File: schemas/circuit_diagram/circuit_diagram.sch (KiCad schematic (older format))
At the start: 10 parts

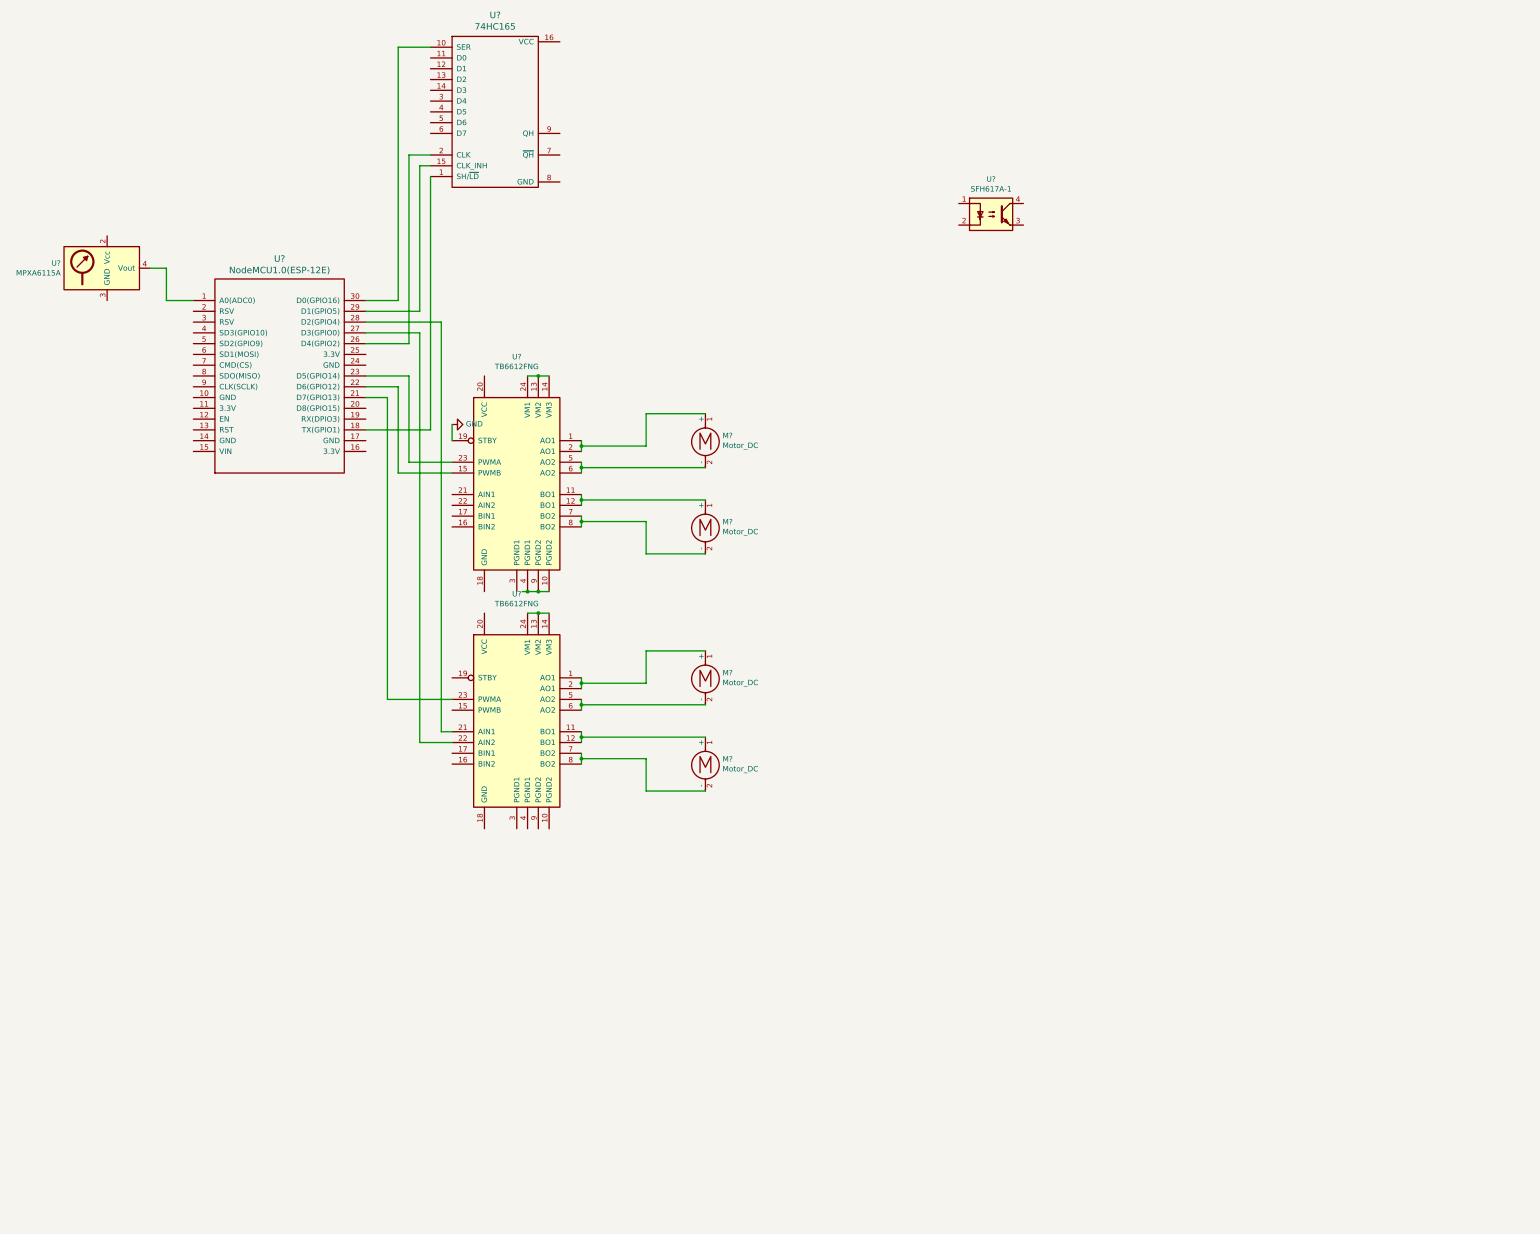
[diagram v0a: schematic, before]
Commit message: schema, and arduino side v_01.1
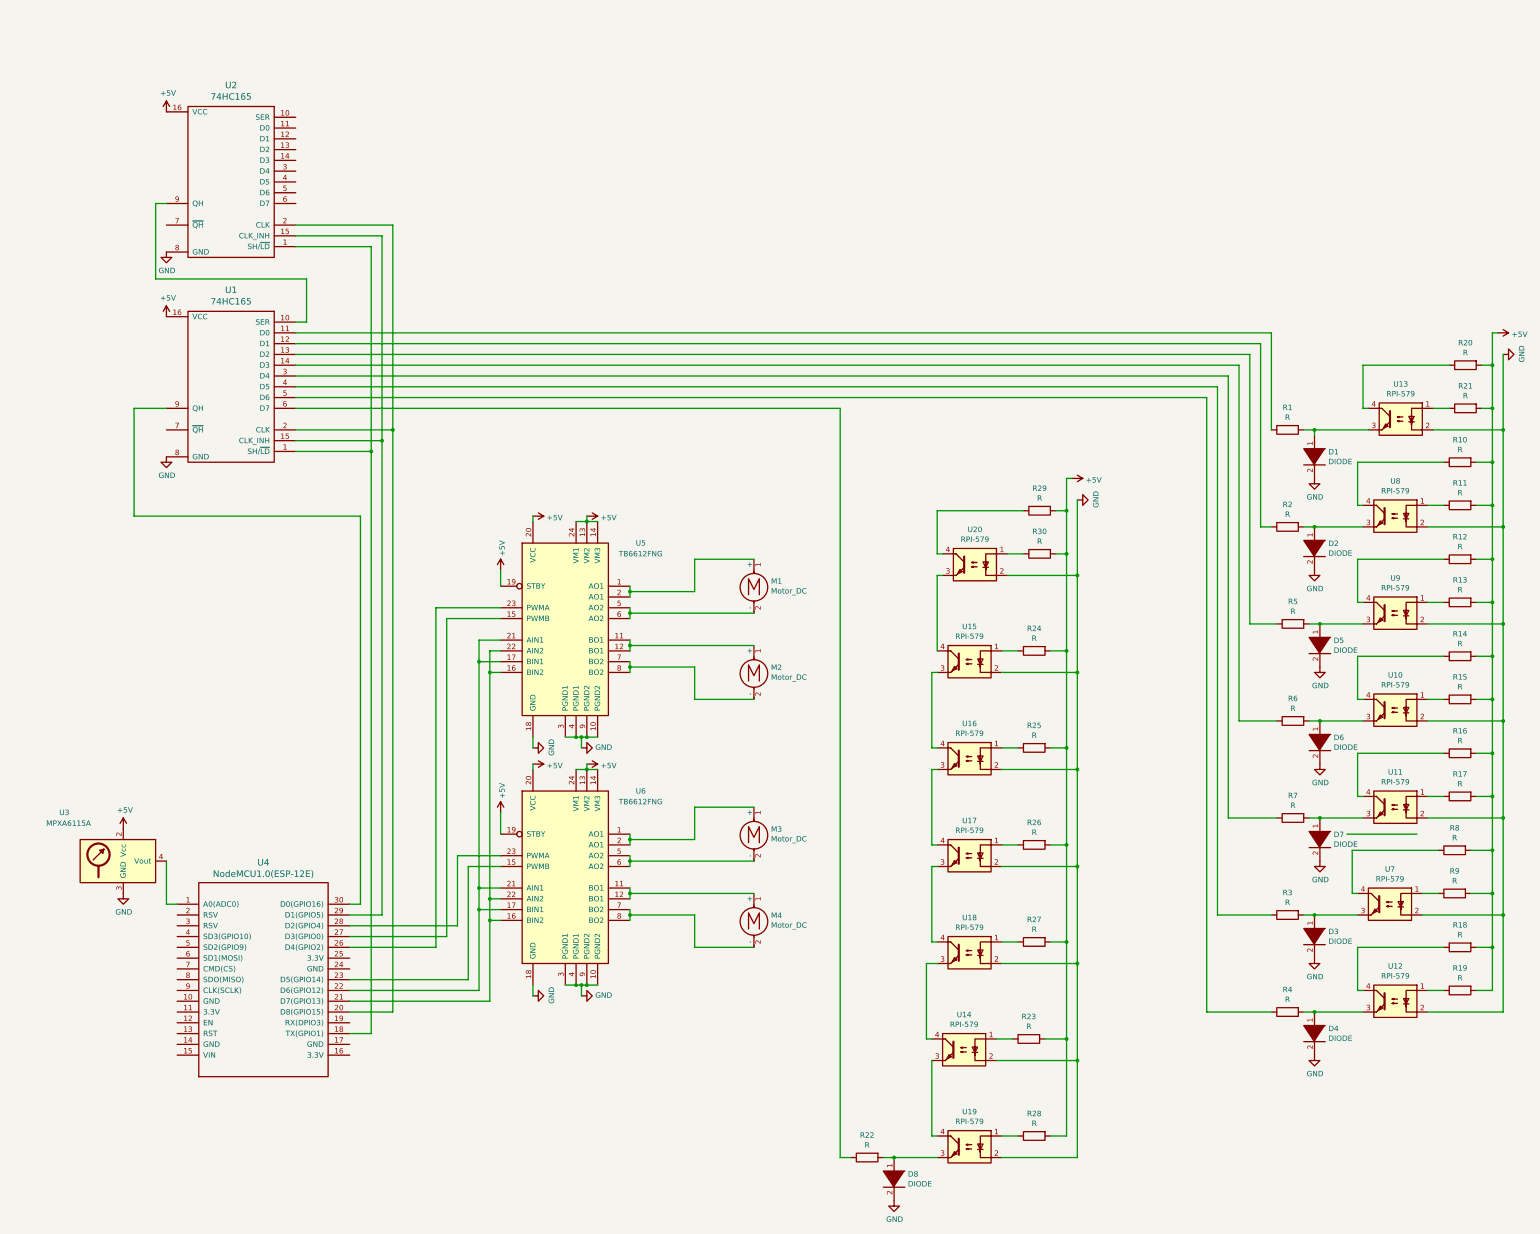
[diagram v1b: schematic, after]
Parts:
- added D1, D2, D3, D4, D5, D6, D7, D8: DIODE, symbol pspice:DIODE
- added R1, R10, R11, R12, R13, R14, R15, R16, R17, R18, R19, R2, R20, R21, R22, R23, R24, R25, R26, R27, R28, R29, R3, R30, R4, R5, R6, R7, R8, R9: R, symbol Device:R
- added U10, U11, U12, U13, U14, U15, U16, U17, U18, U19, U20, U8, U9: RPI-579, Package_DIP:DIP-4_W7.62mm, symbol Isolator:SFH617A-1
- added U2: 74HC165, symbol pkl_misc:74HC165
- U7: renamed from U?; value SFH617A-1 -> RPI-579
- gave numbers to parts that had none: 9
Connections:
- net GND: now also U1.8 (GND), U3.3 (GND), U5.10 (PGND2), U5.18 (GND), U5.3 (PGND1), U5.4 (PGND1), U5.9 (PGND2), U6.10 (PGND2), U6.18 (GND), U6.3 (PGND1), U6.4 (PGND1), U6.9 (PGND2), U7.2, D1.2 (A), D2.2 (A), D3.2 (A), D4.2 (A), D5.2 (A), D6.2 (A), D7.2 (A), D8.2 (A), U10.2, U11.2, U12.2, U13.2, U14.2, U15.2, U16.2, U17.2, U18.2, U19.2, U2.8 (GND), U20.2, U8.2, U9.2; no longer U5.19 (STBY)
- net at U1.1 (SH/~LD), U4.18 (TX(GPIO1)): now also U2.1 (SH/~LD)
- net at U4.20 (D8(GPIO15)): now also U1.2 (CLK), U2.2 (CLK)
- net at U4.21 (D7(GPIO13)): now also U5.16 (BIN2), U5.22 (AIN2), U6.16 (BIN2), U6.22 (AIN2); no longer U6.23 (PWMA)
- net at U4.22 (D6(GPIO12)): now also U5.17 (BIN1), U5.21 (AIN1), U6.17 (BIN1), U6.21 (AIN1); no longer U5.15 (PWMB)
- net at U4.23 (D5(GPIO14)): now also U6.15 (PWMB); no longer U5.23 (PWMA)
- net at U4.26 (D4(GPIO2)): now also U5.23 (PWMA); no longer U1.2 (CLK)
- net at U4.27 (D3(GPIO0)): now also U5.15 (PWMB); no longer U6.22 (AIN2)
- net at U4.28 (D2(GPIO4)): now also U6.23 (PWMA); no longer U6.21 (AIN1)
- net at U1.15 (CLK_INH), U4.29 (D1(GPIO5)): now also U2.15 (CLK_INH)
- net at U4.30 (D0(GPIO16)): now also U1.9 (QH); no longer U1.10 (SER)
- net at U1.11 (D0): now also R1.1
- net at U1.12 (D1): now also R2.1
- net at U1.13 (D2): now also R5.1
- net at U1.14 (D3): now also R6.1
- net +5V: now reaches U1.16 (VCC)
- net +5V: now also U3.2 (Vcc), U5.13 (VM2), U5.14 (VM3), U5.19 (STBY), U5.20 (VCC), U5.24 (VM1), U6.13 (VM2), U6.14 (VM3), U6.19 (STBY), U6.20 (VCC), U6.24 (VM1), R10.2, R11.2, R12.2, R13.2, R14.2, R15.2, R16.2, R17.2, R18.2, R19.2, R20.2, R21.2, R23.2, R24.2, R25.2, R26.2, R27.2, R28.2, R29.2, R30.2, R8.2, R9.2, U2.16 (VCC)
- net at U1.3 (D4): now also R7.1
- net at U1.4 (D5): now also R3.1
- net at U1.5 (D6): now also R4.1
- net at U1.6 (D7): now also R22.1
- net at U7.1: now also R9.1
- net at U7.3: now also D3.1 (K), R3.2
- net at U7.4: now also R8.1
- new net: U1.10 (SER), U2.9 (QH)
- new net: R23.1, U14.1
- new net: U14.3, U19.4
- new net: U14.4, U18.3
- new net: R27.1, U18.1
- new net: U17.3, U18.4
- new net: R26.1, U17.1
- new net: U16.3, U17.4
- new net: R25.1, U16.1
- new net: U15.3, U16.4
- new net: R24.1, U15.1
- new net: U15.4, U20.3
- new net: R30.1, U20.1
- new net: R29.1, U20.4
- new net: R28.1, U19.1
- new net: D8.1 (K), R22.2, U19.3
- new net: R17.1, U11.1
- new net: D7.1 (K), R7.2, U11.3
- new net: R16.1, U11.4
- new net: R15.1, U10.1
- new net: D6.1 (K), R6.2, U10.3
- new net: R14.1, U10.4
- new net: R13.1, U9.1
- new net: D5.1 (K), R5.2, U9.3
- new net: R12.1, U9.4
- new net: R11.1, U8.1
- new net: D2.1 (K), R2.2, U8.3
- new net: R10.1, U8.4
- new net: R21.1, U13.1
- new net: D1.1 (K), R1.2, U13.3
- new net: R20.1, U13.4
- new net: R19.1, U12.1
- new net: D4.1 (K), R4.2, U12.3
- new net: R18.1, U12.4
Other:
- moved on the sheet: M1, M2, M3, M4, U1, U3, U4, U5, U6, U7
